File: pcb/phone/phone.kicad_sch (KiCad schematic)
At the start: 27 parts, among them CN1 S2B-PH-SM4-TB, U4 TPS63021DSJR, U5 TPS7A0218PDBVR, U6 MCP73831-2ACI/MC, U7 MAX17048G+T10

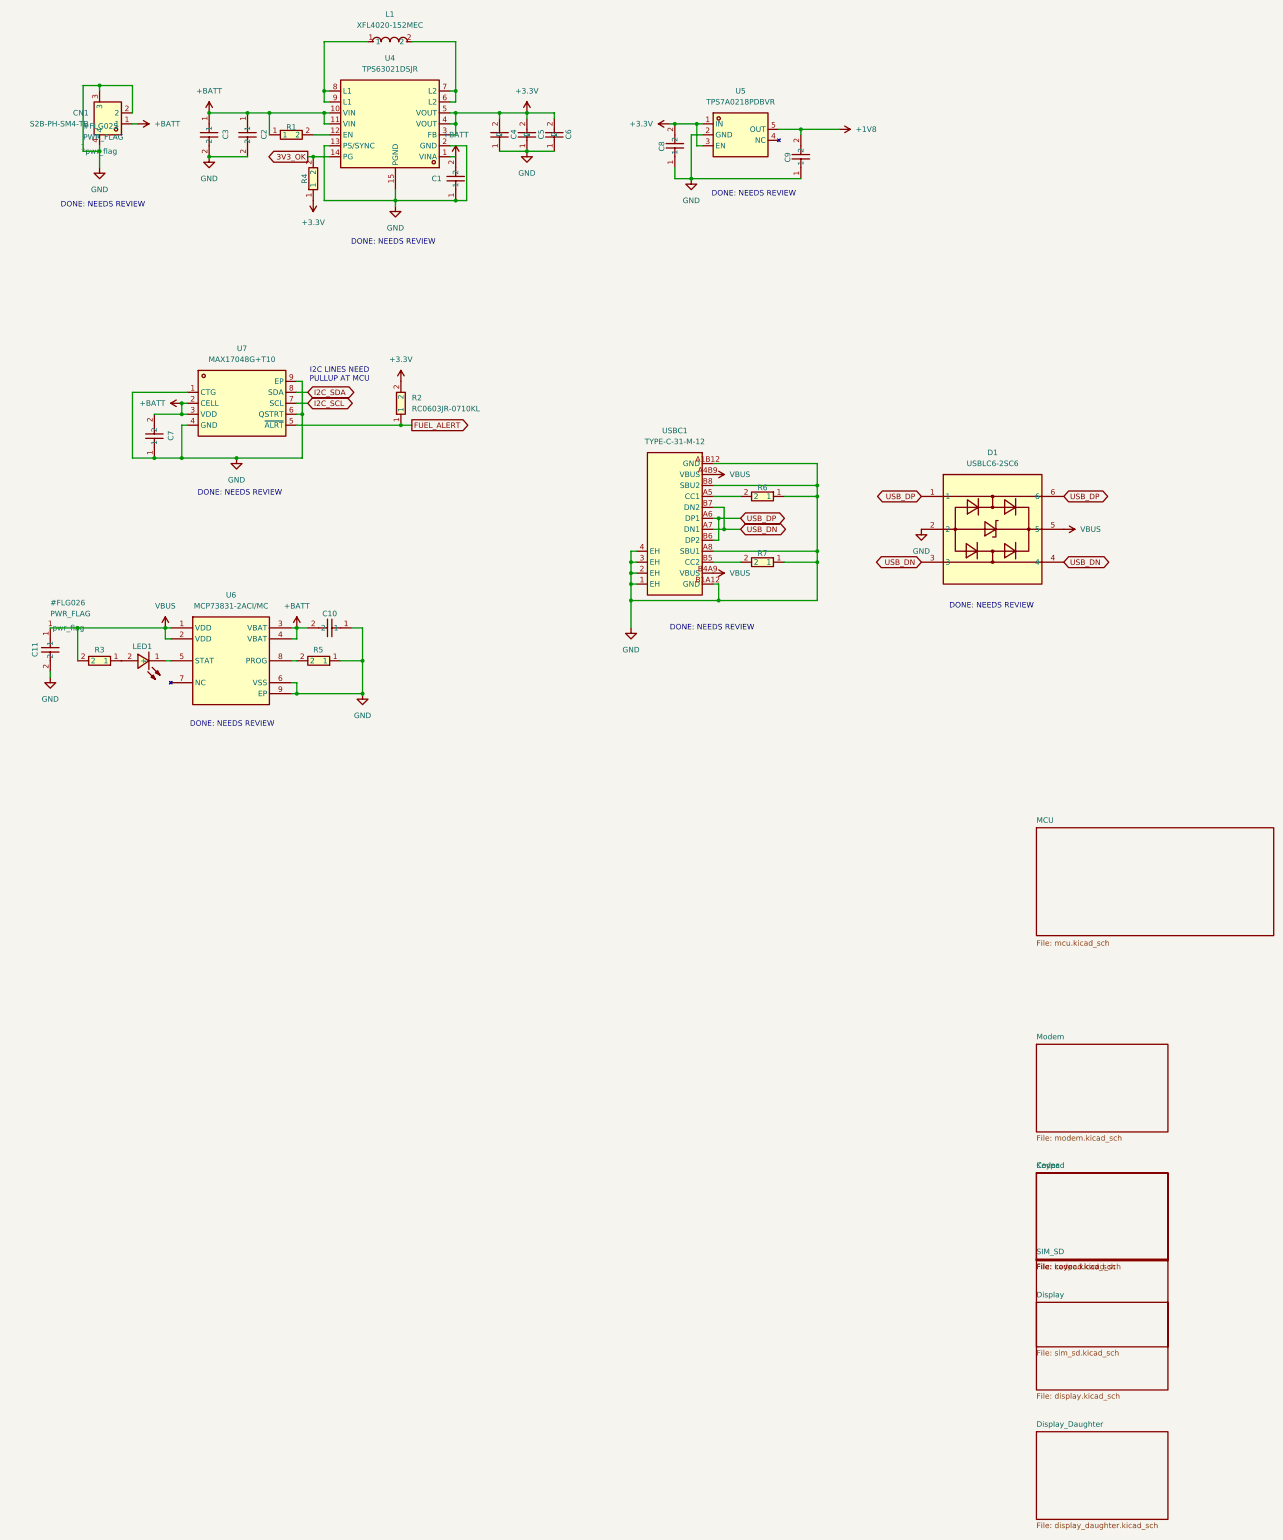
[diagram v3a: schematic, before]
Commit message: Move power section from root sheet to power.kicad_sch sub-sheet
Extracted the entire power section (USBC1, CN1, U4 TPS63021, U5 TPS7A0218,
U6 MCP73831, U7 MAX17048, D1 USBLC6-2, L1, LED1, R1-R7, C1-C11, all power
symbols, PWR_FLAGs, wires, junctions, global labels, text annotations) from
the root sheet (phone.kicad_sch) into a new power.kicad_sch sub-sheet.

Changes:
- Created pcb/phone/power.kicad_sch (UUID 93995179-fee9-4317-80b0-38473b44bbe2)
  with all power components, lib_symbols, wires, junctions, global labels,
  and text annotations moved from the root sheet.
- Updated phone.kicad_sch (root): removed all power components/lib_symbols/
  wires/junctions/labels. Root now contains only the 8 hierarchical sheet
  blocks (Power, Codec, Modem, Display_Daughter, SIM_SD, Keypad, MCU, Display)
  + sheet_instances + embedded_fonts.
- Added Power sheet block to root sheet at (50, 200).
- Updated all symbol instance paths in power.kicad_sch from root path to
  root/power path.
- Updated phone.kicad_pro: added Power to sheets list.

The power section design is unchanged (LOCKED per pcb/AGENTS.md) — this is
purely a structural reorganization. All global labels (VBUS, +BATT, +3.3V,
+1V8, GND, FUEL_ALERT, I2C_SDA/SCL, USB_DP/DN, 3V3_OK) still connect across
sheets via global labels.

ERC: 0 errors, 175 warnings (all pre-existing: 131 endpoint_off_grid,
35 lib_symbol_mismatch, 9 isolated_pin_label). All 9 sheets found.

Generated with [Devin](https://devin.ai)

Co-Authored-By: Devin <158243242+devin-ai-integration[bot]@users.noreply.github.com>
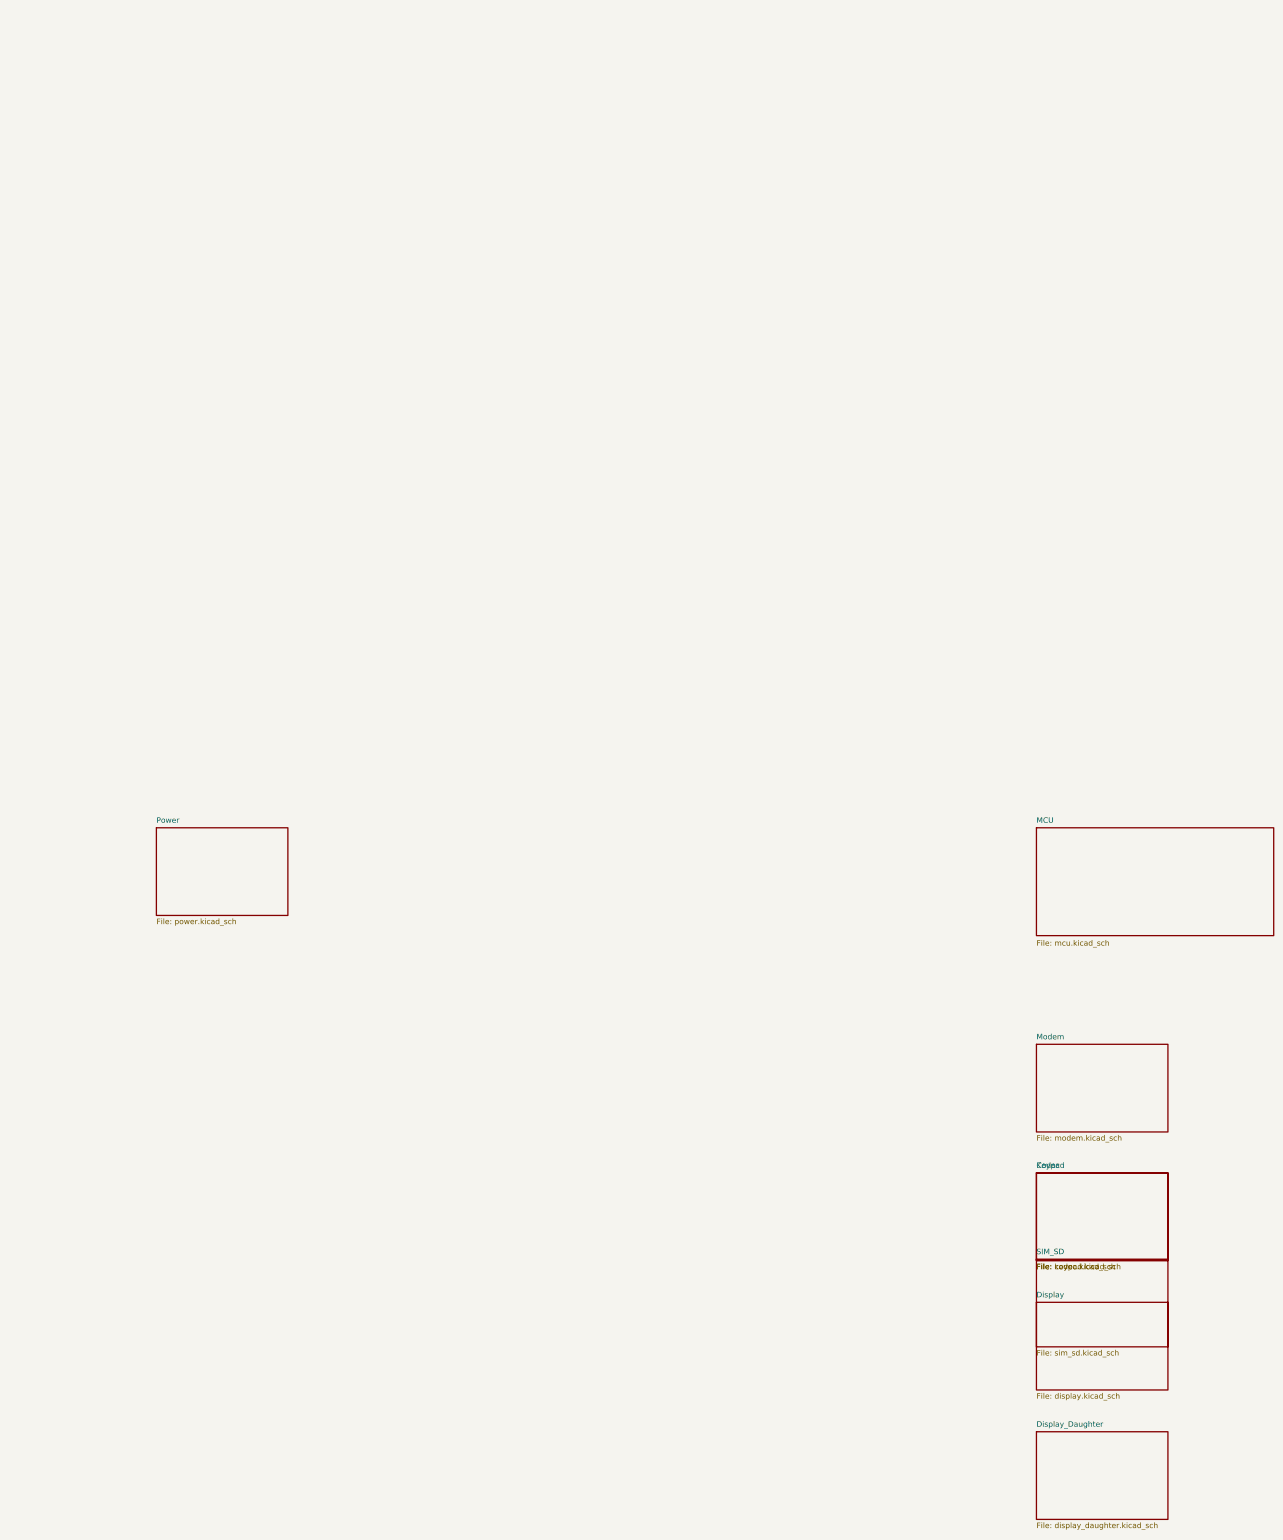
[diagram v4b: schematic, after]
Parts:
- removed C1, C7: CC0603KRX7R9BB104, easyeda2kicad:C0603, symbol passives:CC0603KRX7R9BB104
- removed C10, C11: GRM188R61C475KE11D, easyeda2kicad:C0603, symbol passives:GRM188R61C475KE11D
- removed C2, C3: GRM21BR61H106KE43L, easyeda2kicad:C0805, symbol passives:GRM21BR61H106KE43L
- removed C4, C5, C6: GRM21BR61A226ME51L, easyeda2kicad:C0805, symbol passives:GRM21BR61A226ME51L
- removed C8, C9: GRM188R61C105KA93D, easyeda2kicad:C0603, symbol passives:GRM188R61C105KA93D
- removed CN1: S2B-PH-SM4-TB, easyeda2kicad:CONN-SMD_P2.00_S2B-PH-SM4-TB-LF-SN, symbol connectors:S2B-PH-SM4-TB
- removed D1: USBLC6-2SC6, easyeda2kicad:SOT-23-6_L2.9-W1.6-P0.95-LS2.8-BL, symbol ics:USBLC6-2SC6
- removed L1: XFL4020-152MEC, easyeda2kicad:IND-SMD_L4.0-W4.0-A, symbol passives:XFL4020-152MEC
- removed LED1: LTST-C191TBKT, easyeda2kicad:LED0603-RD, symbol passives:LTST-C191TBKT
- removed R1: RC0603JR-071ML, easyeda2kicad:R0603, symbol passives:RC0603JR-071ML
- removed R2, R4: RC0603JR-0710KL, easyeda2kicad:R0603, symbol passives:RC0603JR-0710KL
- removed R3: RC0603JR-07470RL, easyeda2kicad:R0603, symbol passives:RC0603JR-07470RL
- removed R5: RC0603FR-072KL, easyeda2kicad:R0603, symbol passives:RC0603FR-072KL
- removed R6, R7: RC0603FR-075K1L, easyeda2kicad:R0603, symbol passives:RC0603FR-075K1L
- removed U4: TPS63021DSJR, easyeda2kicad:VSON-14_L4.0-W3.0-P0.50-BL-EP_TI_DSJ, symbol ics:TPS63021DSJR
- removed U5: TPS7A0218PDBVR, easyeda2kicad:SOT-23-5_L2.9-W1.6-P0.95-LS2.8-BL, symbol ics:TPS7A0218PDBVR
- removed U6: MCP73831-2ACI/MC, easyeda2kicad:TDFN-8_L3.0-W2.0-P0.50-BL-EP1.6, symbol ics:MCP73831-2ACI_MC
- removed U7: MAX17048G+T10, easyeda2kicad:TDFN-8_L2.0-W2.0-P0.50-BL-EP1.2, symbol ics:MAX17048G+T10
- removed USBC1: TYPE-C-31-M-12, easyeda2kicad:USB-C_SMD-TYPE-C-31-M-12_1, symbol connectors:TYPE-C-31-M-12
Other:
- added sheet Power (power.kicad_sch)
- note removed: "DONE: NEEDS REVIEW"
- note removed: "I2C LINES NEED PULLUP AT MCU"

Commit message: Cleanup: remove rejected part symbols, one-off scripts, stale datasheets
- Remove 7 rejected symbols from easyeda2kicad.kicad_sym (PJ-327C-4A,
  PJ-3250-5A, PJ-3240-5A, TYPE-C16PLC-H10.0, PJ-327A5JJ, PJ-327-P5,
  TYPEC-306DDW-ARP16) — replaced by Tensility 54-00298 and GCT USB4085-GF-A
- Delete 10 one-off inspection scripts (check_*.py, find_*.py, dump_*.py,
  extract_*.py) — keep only gen_*.py schematic generators
- Delete rejected datasheets (pj3126-5a, pj3240-5a, pj3250-5a, pj3f07-5p,
  N114 superseded display)
- Delete generated BOM/POS CSV files
- Add alps-ssss2.pdf and gct-usb4085.pdf to reference README index
- Include all schematic changes from previous sessions (SD pullups, VBUS
  divider fix, level shifter verification, codec caps, DCVDD fix)

Generated with [Devin](https://devin.ai)

Co-Authored-By: Devin <158243242+devin-ai-integration[bot]@users.noreply.github.com>
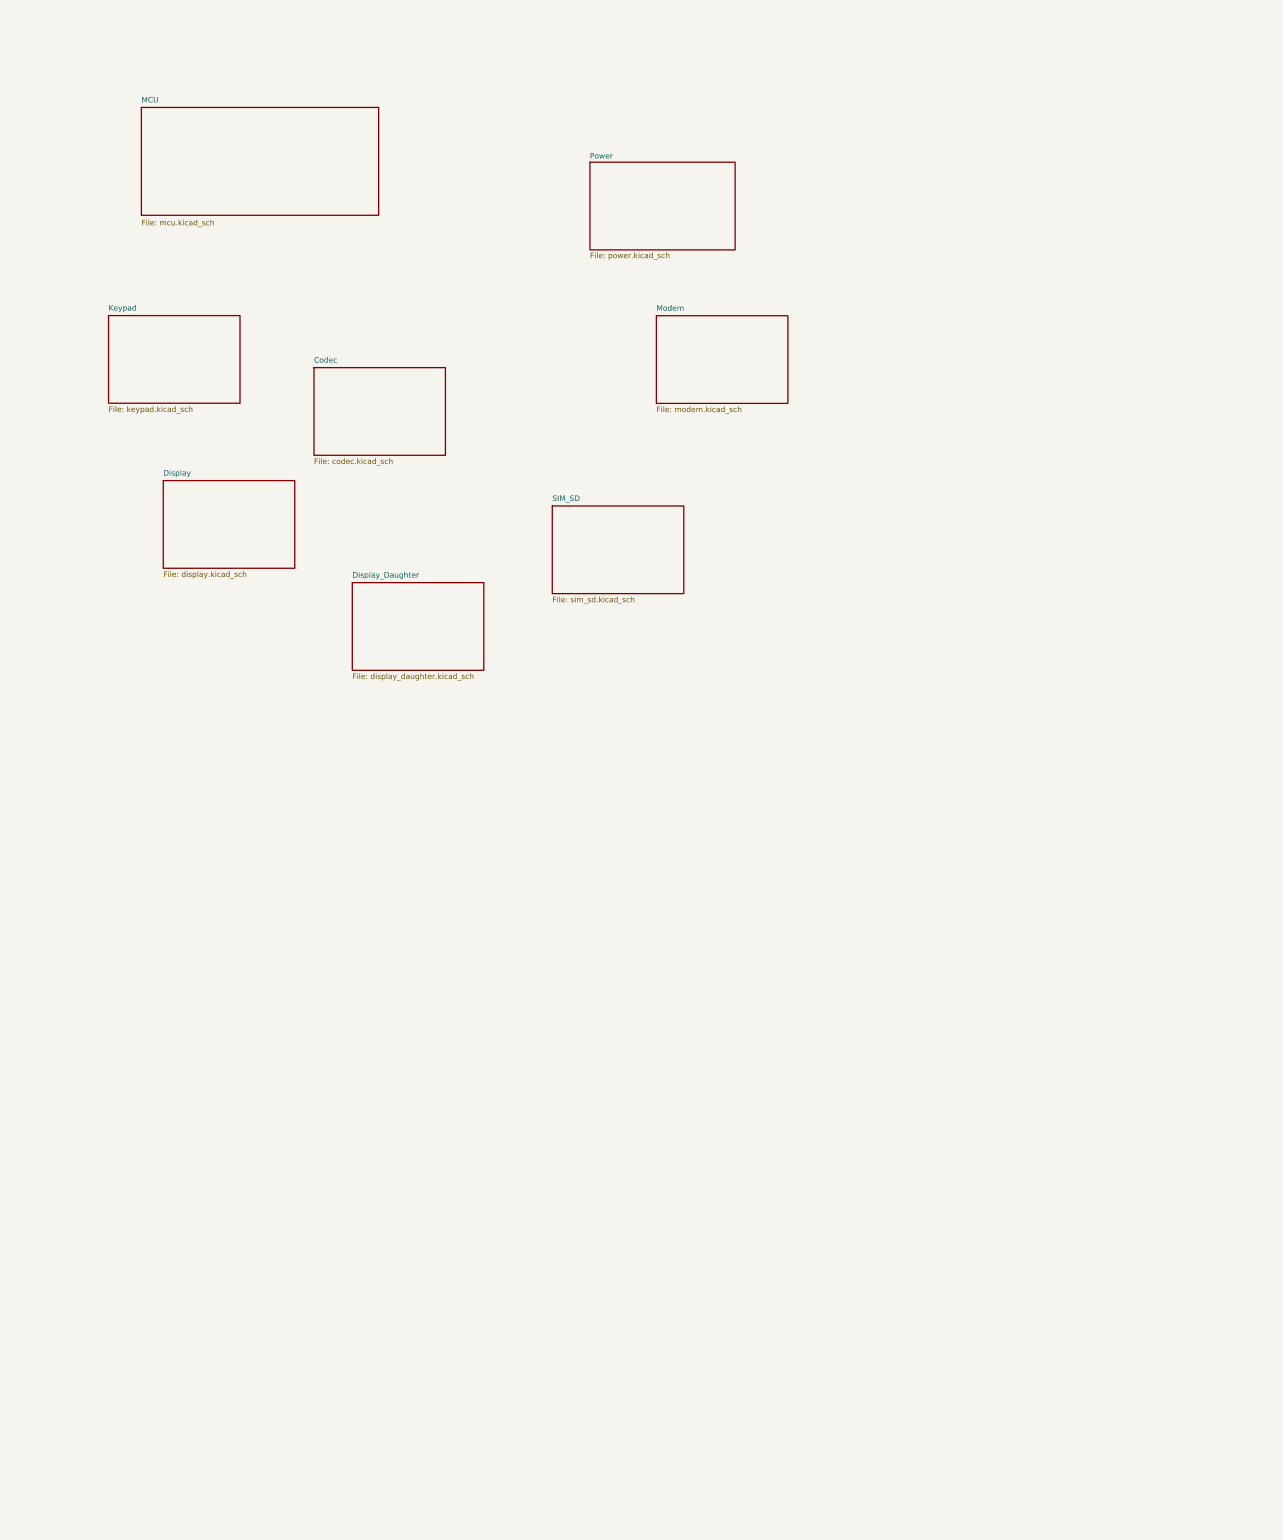
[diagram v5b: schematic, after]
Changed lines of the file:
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@@
 	(paper "A4")
 	(sheet
-		(at 254 280)
+		(at 86.525 93.335)
 		(size 30.48 20.32)
 		(exclude_from_sim no)
@@
 		)
 		(property "Sheetname" "Codec"
-			(at 254 279 0)
+			(at 86.525 92.335 0)
 			(show_name no)
 			(do_not_autoplace no)
@@
 		)
 		(property "Sheetfile" "codec.kicad_sch"
-			(at 254 301 0)
+			(at 86.525 114.335 0)
 			(show_name no)
 			(do_not_autoplace no)
@@
 	)
 	(sheet
-		(at 254 250.19)
+		(at 165.9 81.305)
 		(size 30.48 20.32)
 		(exclude_from_sim no)
@@
 		)
 		(property "Sheetname" "Modem"
-			(at 254 249.19 0)
+			(at 165.9 80.305 0)
 			(show_name no)
 			(do_not_autoplace no)
@@
 		)
 		(property "Sheetfile" "modem.kicad_sch"
-			(at 254 271.19 0)
+			(at 165.9 102.305 0)
 			(show_name no)
 			(do_not_autoplace no)
@@
 	)
 	(sheet
-		(at 254 340)
+		(at 95.415 143.175)
 		(size 30.48 20.32)
 		(exclude_from_sim no)
@@
 		)
 		(property "Sheetname" "Display_Daughter"
-			(at 254 339 0)
+			(at 95.415 142.175 0)
 			(show_name no)
 			(do_not_autoplace no)
@@
 		)
 		(property "Sheetfile" "display_daughter.kicad_sch"
-			(at 254 361 0)
+			(at 95.415 164.175 0)
 			(show_name no)
 			(do_not_autoplace no)
@@
 	)
 	(sheet
-		(at 254 300)
+		(at 141.77 125.4)
 		(size 30.48 20.32)
 		(exclude_from_sim no)
@@
 		)
 		(property "Sheetname" "SIM_SD"
-			(at 254 299 0)
+			(at 141.77 124.4 0)
 			(show_name no)
 			(do_not_autoplace no)
@@
 		)
 		(property "Sheetfile" "sim_sd.kicad_sch"
-			(at 254 321 0)
+			(at 141.77 146.4 0)
 			(show_name no)
 			(do_not_autoplace no)
@@
 	)
 	(sheet
-		(at 254 280)
+		(at 150.495 45.72)
+		(size 33.655 20.32)
+		(exclude_from_sim no)
+		(in_bom yes)
+		(on_board yes)
+		(dnp no)
+		(fields_autoplaced yes)
+		(stroke
+			(width 0.1524)
+			(type solid)
+		)
+		(fill
+			(color 0 0 0 0)
+		)
+		(property "Sheetname" "Power"
+			(at 150.495 45.0084 0)
+			(show_name no)
+			(do_not_autoplace no)
+			(effects
+				(font
+					(size 1.27 1.27)
+				)
+				(justify left bottom)
+			)
+		)
+		(property "Sheetfile" "power.kicad_sch"
+			(at 150.495 66.6246 0)
+			(show_name no)
+			(do_not_autoplace no)
+			(effects
+				(font
+					(size 1.27 1.27)
+				)
+				(justify left top)
+			)
+		)
+		(instances
+			(project "phone"
+				(path "/451c3b43-1616-42cb-bf96-d436f4db82c2"
+					(page "8")
+				)
+			)
+		)
+	)
+	(sheet
+		(at 38.9 81.27)
 		(size 30.48 20.32)
 		(exclude_from_sim no)
@@
 		)
 		(property "Sheetname" "Keypad"
-			(at 254 279 0)
+			(at 38.9 80.27 0)
 			(show_name no)
 			(do_not_autoplace no)
@@
 		)
 		(property "Sheetfile" "keypad.kicad_sch"
-			(at 254 301 0)
+			(at 38.9 102.27 0)
 			(show_name no)
 			(do_not_autoplace no)
@@
 	)
 	(sheet
-		(at 254 200)
+		(at 46.52 33.02)
 		(size 55 25)
 		(exclude_from_sim no)
@@
 		)
 		(property "Sheetname" "MCU"
-			(at 254 199 0)
+			(at 46.52 32.02 0)
 			(show_name no)
 			(do_not_autoplace no)
@@
 		)
 		(property "Sheetfile" "mcu.kicad_sch"
-			(at 254 226 0)
+			(at 46.52 59.02 0)
 			(show_name no)
 			(do_not_autoplace no)
@@
 	)
 	(sheet
-		(at 254 310)
+		(at 51.6 119.525)
 		(size 30.48 20.32)
 		(exclude_from_sim no)
@@
 		)
 		(property "Sheetname" "Display"
-			(at 254 309 0)
+			(at 51.6 118.525 0)
 			(show_name no)
 			(do_not_autoplace no)
@@
 		)
 		(property "Sheetfile" "display.kicad_sch"
-			(at 254 331 0)
+			(at 51.6 140.525 0)
 			(show_name no)
 			(do_not_autoplace no)
@@
 				)
 			)
-		)
-	)
-	(sheet
-		(at 50 200)
-		(size 30.48 20.32)
-		(exclude_from_sim no)
-		(in_bom yes)
-		(on_board yes)
-		(dnp no)
-		(fields_autoplaced yes)
-		(stroke
-			(width 0.1524)
-			(type solid)
-		)
-		(fill
-			(color 0 0 0 0)
-		)
-		(property "Sheetname" "Power"
-			(at 50 199 0)
-			(show_name no)
-			(do_not_autoplace no)
-			(effects
-				(font
-					(size 1.27 1.27)
-				)
-				(justify left bottom)
-			)
-		)
-		(property "Sheetfile" "power.kicad_sch"
-			(at 50 221 0)
-			(show_name no)
-			(do_not_autoplace no)
-			(effects
-				(font
-					(size 1.27 1.27)
-				)
-				(justify left top)
-			)
-		)
-		(instances
-			(project "phone"
-				(path "/451c3b43-1616-42cb-bf96-d436f4db82c2"
-					(page "8")
-				)
-			)

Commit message: Fix top-level sheet: page numbering, title block, doc sync
- Fix duplicate page number: Keypad was page 4 (same as Codec),
  renumbered to page 9. Pages now unique 1-9 across all sheets.
- Add title block to root sheet with project metadata (title,
  date, rev, architecture summary comments).
- Update block-diagram.md: document actual hierarchical schematic
  approach (was stale — said "flat, no hierarchical sheets").
  Old text struck through and marked SUPERSEDED.
- Fix 3D model paths in 2 footprints (temp_470uf/temp_switch ->
  easyeda2kicad) to complete the library merge from prior commit.

ERC validated: 0 errors, 15 warnings (all pre-existing, unchanged).

Generated with [Devin](https://devin.ai)

Co-Authored-By: Devin <158243242+devin-ai-integration[bot]@users.noreply.github.com>
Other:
- title: (none) -> Custom Cell Phone
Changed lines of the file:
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@@
 	(generator_version "10.0")
 	(paper "A4")
+	(title_block
+		(title "Custom Cell Phone")
+		(date "2026-07-28")
+		(rev "Rev 1")
+		(company "")
+		(comment 1 "STM32H743ZI + SIM7600NA-H + ALC5651 + Zephyr RTOS")
+		(comment 2 "Hierarchical schematic — 8 sub-sheets, global labels for inter-sheet nets")
+	)
 	(sheet
 		(at 86.525 93.335)
@@
 			(project "phone"
 				(path "/451c3b43-1616-42cb-bf96-d436f4db82c2"
-					(page "4")
-				)
-			)
+					(page "9")
+				)
+			)
